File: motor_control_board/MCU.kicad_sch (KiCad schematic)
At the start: 17 parts

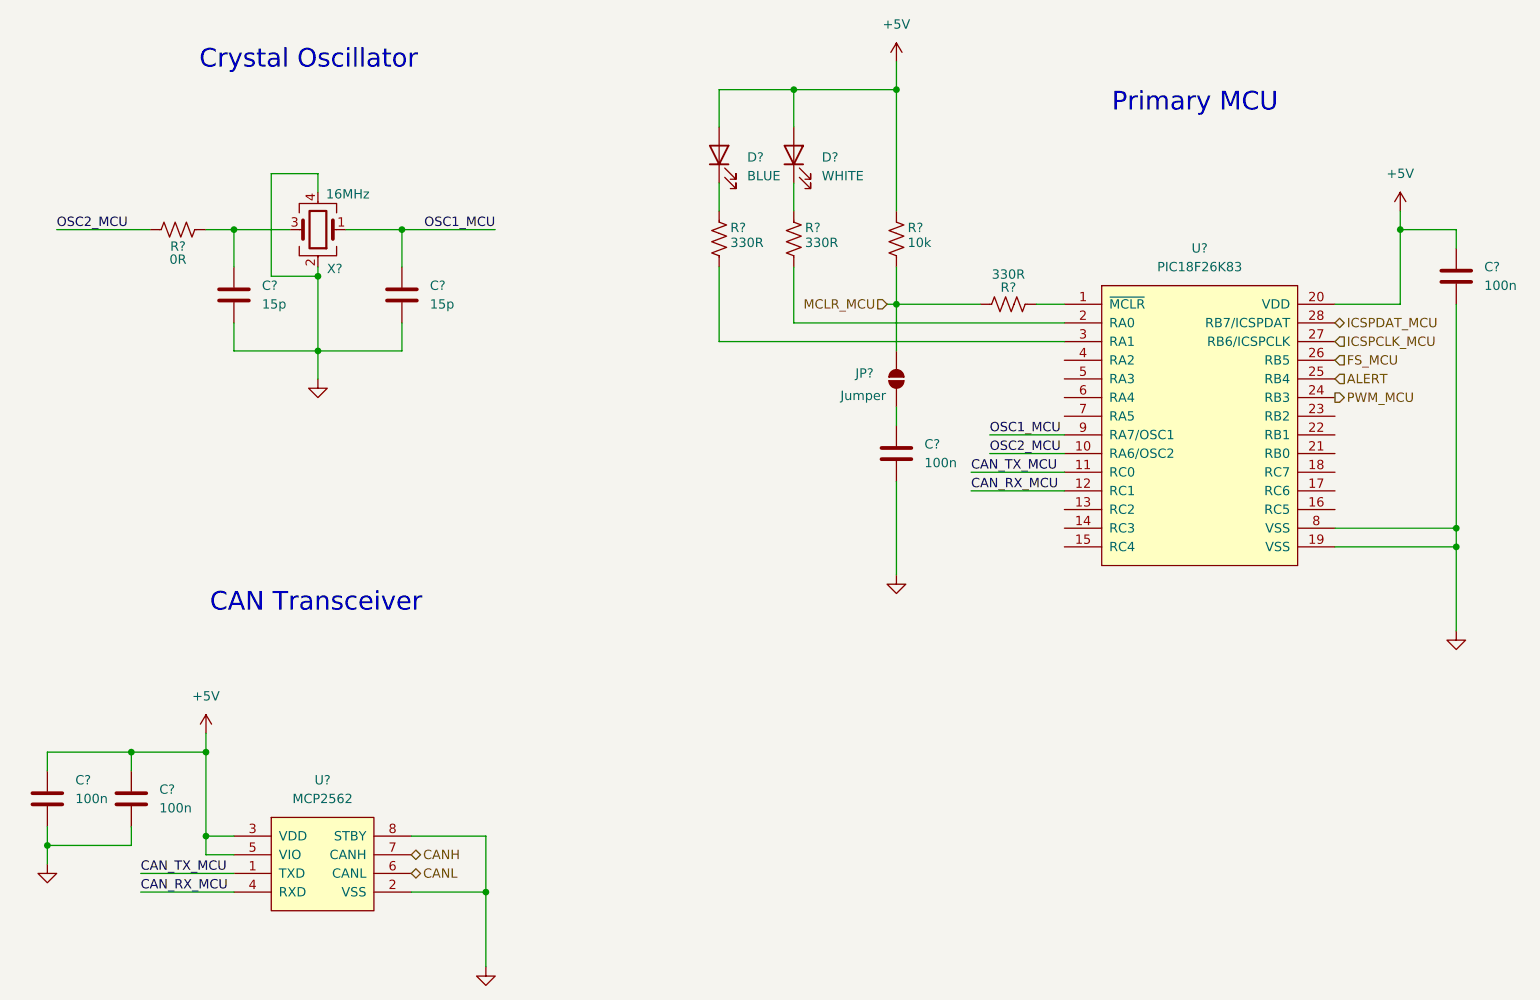
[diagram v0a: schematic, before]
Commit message: Minor schematic edits
Annotated schematic, selected mosfet and diodes, addressed comments
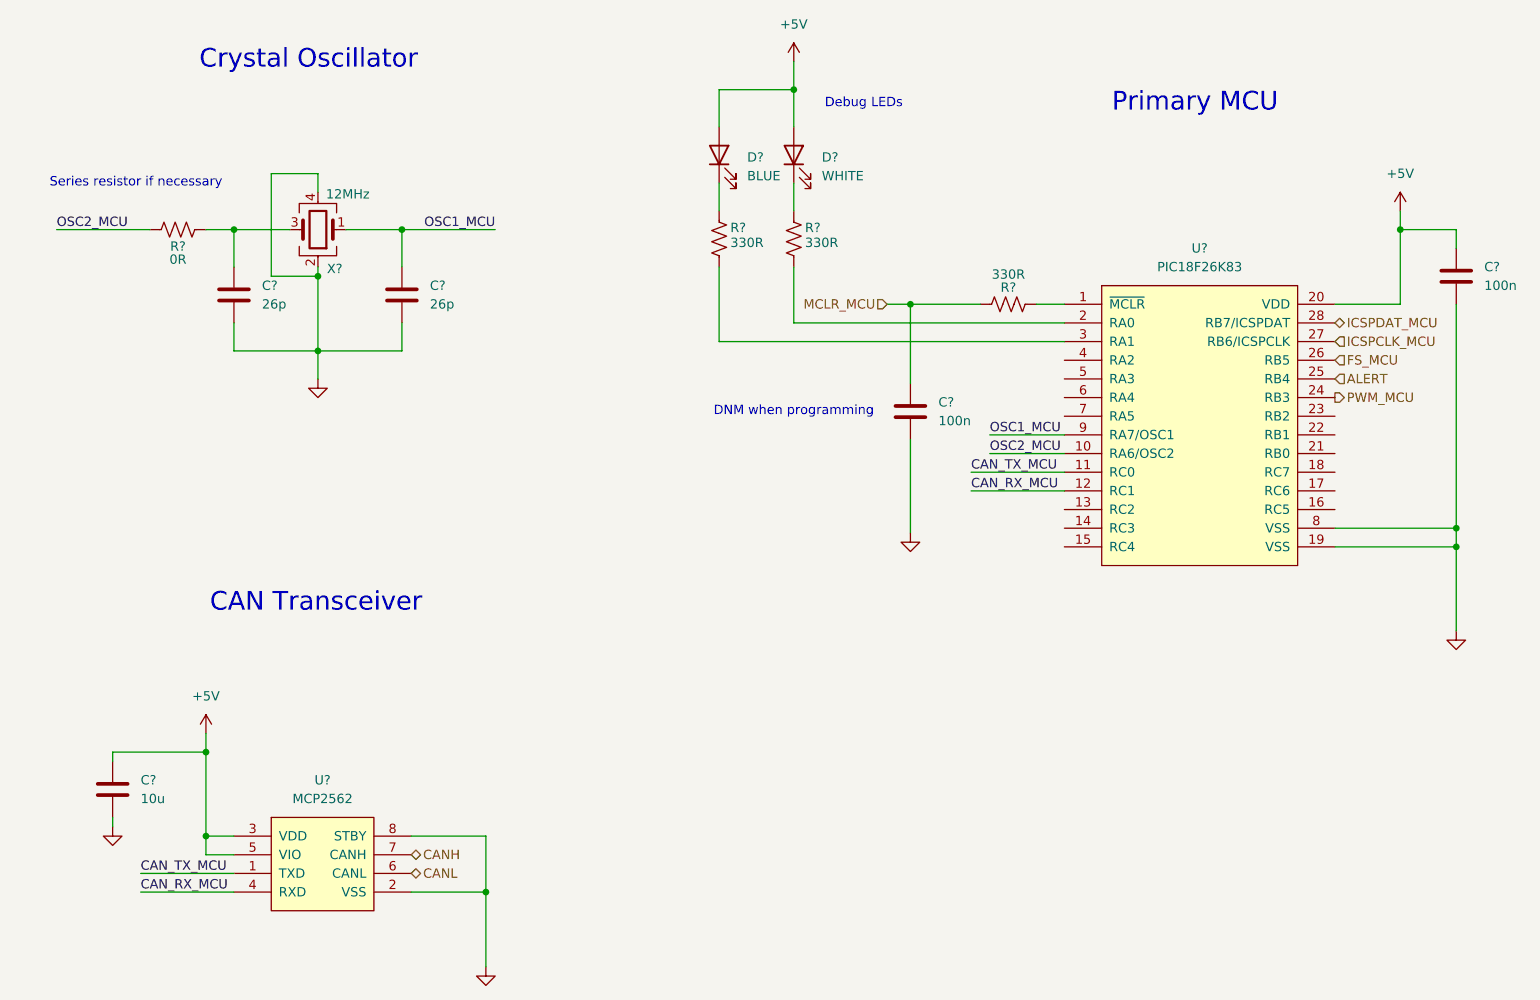
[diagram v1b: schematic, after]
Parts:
- removed C?: 100n, symbol canhw:C
- removed JP?: Jumper, symbol canhw:SolderJumper_2_Open
- removed R?: 10k, symbol canhw:R_US
- C?: value 100n -> 10u
- C? (x2): value 15p -> 26p
- X?: value 16MHz -> 12MHz
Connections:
- net MCLR_MCU: now also C?.1
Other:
- note added: "DNM when programming"
- note added: "Debug LEDs"
- note added: "Series resistor if necessary"
- moved on the sheet: C?

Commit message: Added second encoder connection, minor edits
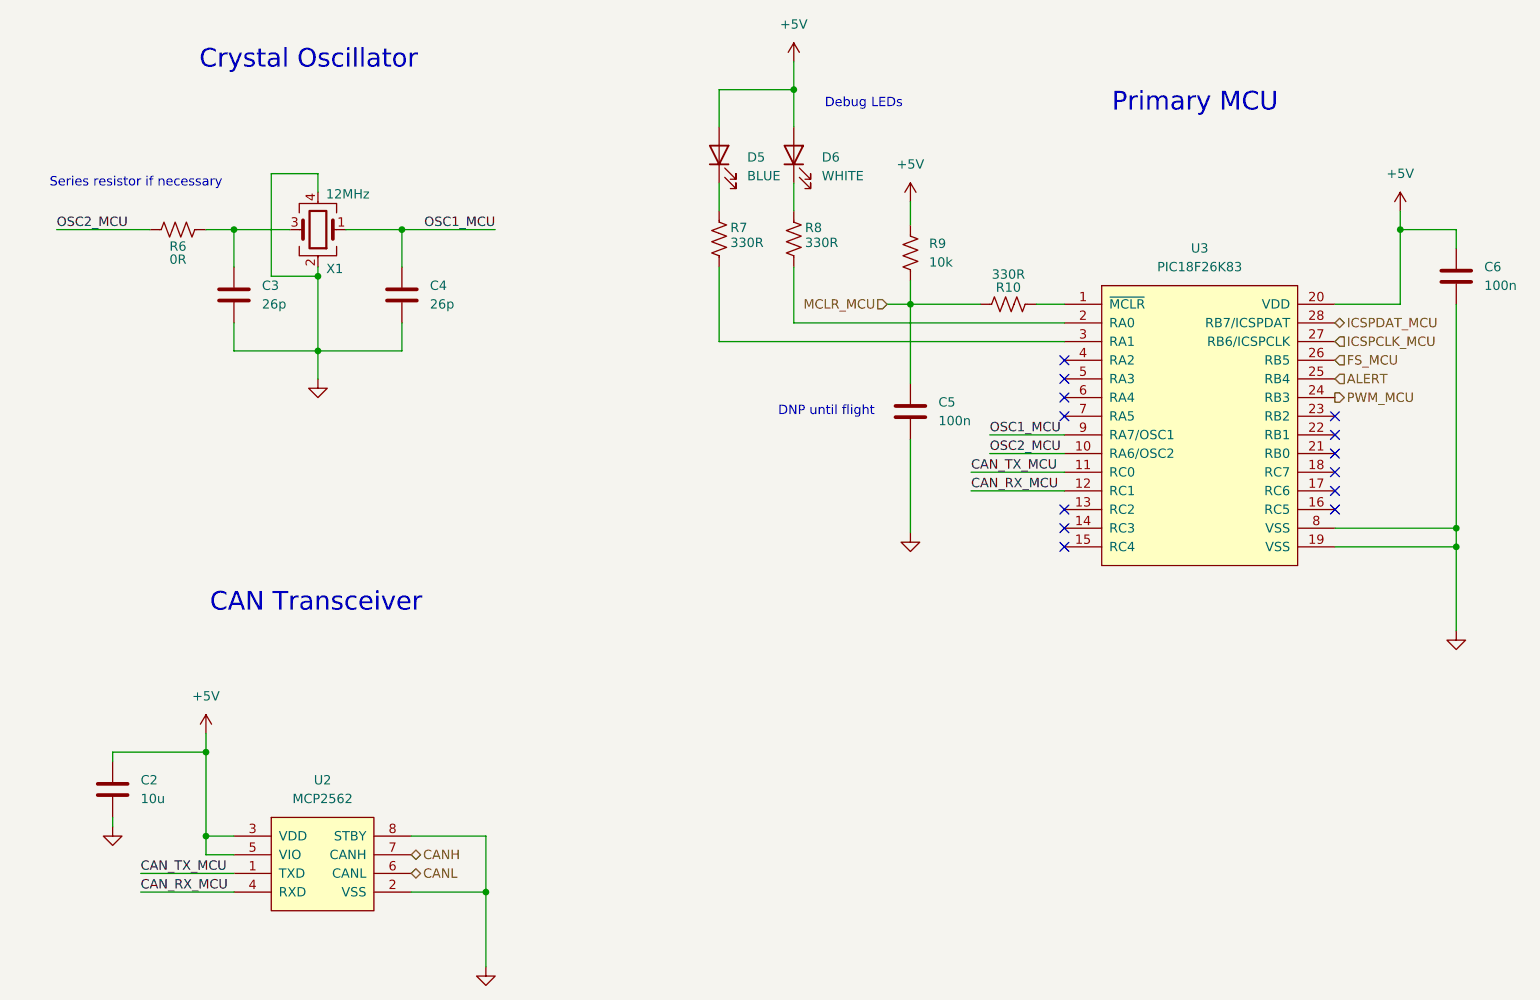
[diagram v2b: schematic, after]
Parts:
- added R9: 10k, symbol Device:R_US
- gave numbers to parts that had none: 14
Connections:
- net +5V: now also R9.1
- net MCLR_MCU: now also R9.2
- no-connect marks 0 -> 13
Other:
- note added: "DNP until flight"
- note removed: "DNM when programming"

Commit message: assigned footprints
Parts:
- C2, C3, C4, C5, C6: footprint (none) -> Capacitor_SMD:C_0805_2012Metric_Pad1.18x1.45mm_HandSolder
- D5, D6: footprint (none) -> LED_SMD:LED_1206_3216Metric_Pad1.42x1.75mm_HandSolder
- R10, R6, R7, R8, R9: footprint (none) -> Resistor_SMD:R_0805_2012Metric_Pad1.20x1.40mm_HandSolder
- U2: footprint (none) -> Package_SO:SOIC-8_3.9x4.9mm_P1.27mm
- U3: footprint (none) -> Package_SO:SSOP-28_5.3x10.2mm_P0.65mm
- X1: footprint Crystal:Crystal_SMD_2016-4Pin_2.0x1.6mm -> Crystal:Crystal_SMD_Abracon_ABM8G-4Pin_3.2x2.5mm
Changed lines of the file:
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@@
 			)
 		)
-		(property "Footprint" ""
+		(property "Footprint" "Capacitor_SMD:C_0805_2012Metric_Pad1.18x1.45mm_HandSolder"
 			(at 47.9552 151.13 0)
 			(effects
@@
 			)
 		)
-		(property "Footprint" ""
+		(property "Footprint" "LED_SMD:LED_1206_3216Metric_Pad1.42x1.75mm_HandSolder"
 			(at 139.7 60.96 0)
 			(effects
@@
 			)
 		)
-		(property "Footprint" ""
+		(property "Footprint" "Capacitor_SMD:C_0805_2012Metric_Pad1.18x1.45mm_HandSolder"
 			(at 230.8352 81.28 0)
 			(effects
@@
 			)
 		)
-		(property "Footprint" ""
+		(property "Footprint" "Capacitor_SMD:C_0805_2012Metric_Pad1.18x1.45mm_HandSolder"
 			(at 64.4652 83.82 0)
 			(effects
@@
 			)
 		)
-		(property "Footprint" ""
+		(property "Footprint" "Capacitor_SMD:C_0805_2012Metric_Pad1.18x1.45mm_HandSolder"
 			(at 156.5402 99.695 0)
 			(effects
@@
 			)
 		)
-		(property "Footprint" "Crystal:Crystal_SMD_2016-4Pin_2.0x1.6mm"
+		(property "Footprint" "Crystal:Crystal_SMD_Abracon_ABM8G-4Pin_3.2x2.5mm"
 			(at 74.93 71.12 0)
 			(effects
@@
 			)
 		)
-		(property "Footprint" ""
+		(property "Footprint" "Package_SO:SOIC-8_3.9x4.9mm_P1.27mm"
 			(at 76.2 153.67 0)
 			(effects
@@
 			)
 		)
-		(property "Footprint" ""
+		(property "Footprint" "Capacitor_SMD:C_0805_2012Metric_Pad1.18x1.45mm_HandSolder"
 			(at 87.3252 83.82 0)
 			(effects
@@
 			)
 		)
-		(property "Footprint" ""
+		(property "Footprint" "Resistor_SMD:R_0805_2012Metric_Pad1.20x1.40mm_HandSolder"
 			(at 56.134 70.104 90)
 			(effects
@@
 			)
 		)
-		(property "Footprint" ""
+		(property "Footprint" "Resistor_SMD:R_0805_2012Metric_Pad1.20x1.40mm_HandSolder"
 			(at 168.656 82.296 90)
 			(effects
@@
 			)
 		)
-		(property "Footprint" ""
+		(property "Footprint" "Resistor_SMD:R_0805_2012Metric_Pad1.20x1.40mm_HandSolder"
 			(at 130.556 72.644 90)
 			(effects
@@
 			)
 		)
-		(property "Footprint" ""
+		(property "Footprint" "Resistor_SMD:R_0805_2012Metric_Pad1.20x1.40mm_HandSolder"
 			(at 140.716 72.644 90)
 			(effects
@@
 			)
 		)
-		(property "Footprint" ""
+		(property "Footprint" "Package_SO:SSOP-28_5.3x10.2mm_P0.65mm"
 			(at 207.01 97.79 0)
 			(effects
@@
 			)
 		)
-		(property "Footprint" ""
+		(property "Footprint" "Resistor_SMD:R_0805_2012Metric_Pad1.20x1.40mm_HandSolder"
 			(at 156.591 74.549 90)
 			(effects
@@
 			)
 		)
-		(property "Footprint" ""
+		(property "Footprint" "LED_SMD:LED_1206_3216Metric_Pad1.42x1.75mm_HandSolder"
 			(at 129.54 60.96 0)
 			(effects

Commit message: components placed
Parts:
- D5: value BLUE -> GREEN
- D6: value WHITE -> RED
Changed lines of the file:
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@@
 			)
 		)
-		(property "Value" "WHITE"
+		(property "Value" "RED"
 			(at 143.51 63.8174 90)
 			(effects
@@
 			)
 		)
-		(property "Value" "BLUE"
+		(property "Value" "GREEN"
 			(at 133.35 63.8174 90)
 			(effects

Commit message: Fixed symbol and footprint libraries
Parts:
- R9: symbol Device:R_US -> canhw:R_US
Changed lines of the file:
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@@
 	)
 	(symbol
-		(lib_id "Device:R_US")
+		(lib_id "canhw:R_US")
 		(at 155.575 74.295 0)
 		(unit 1)
